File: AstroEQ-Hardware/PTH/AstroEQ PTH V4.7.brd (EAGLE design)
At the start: 100 x 66 mm, 54 parts, among them IC1 DIP40-SOCKET, IC2 DIP20-SOCKET, IC3 78L05, J2 DNI, J3 DNI, M1 Motor Driver, M2 Motor Driver, Q1 NTR4501NT1G, X1 16MHz, X2 12MHz

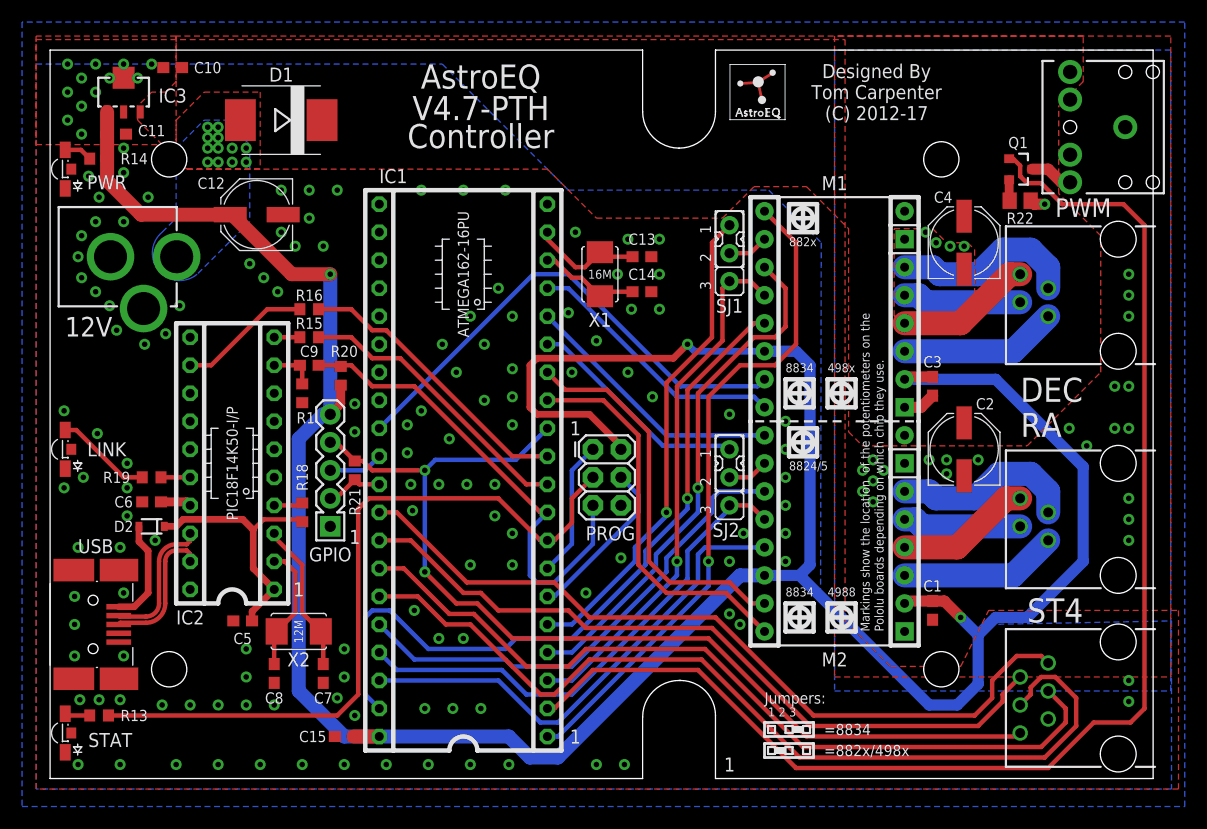
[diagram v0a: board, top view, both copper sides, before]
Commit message: Update AstroEQ PTH/SMD Schematics
1. Tidy up the schematics, add a frame, and improve labelling of nets
2. Add extra textual documentation to the PCB to label the various extra IO pins.
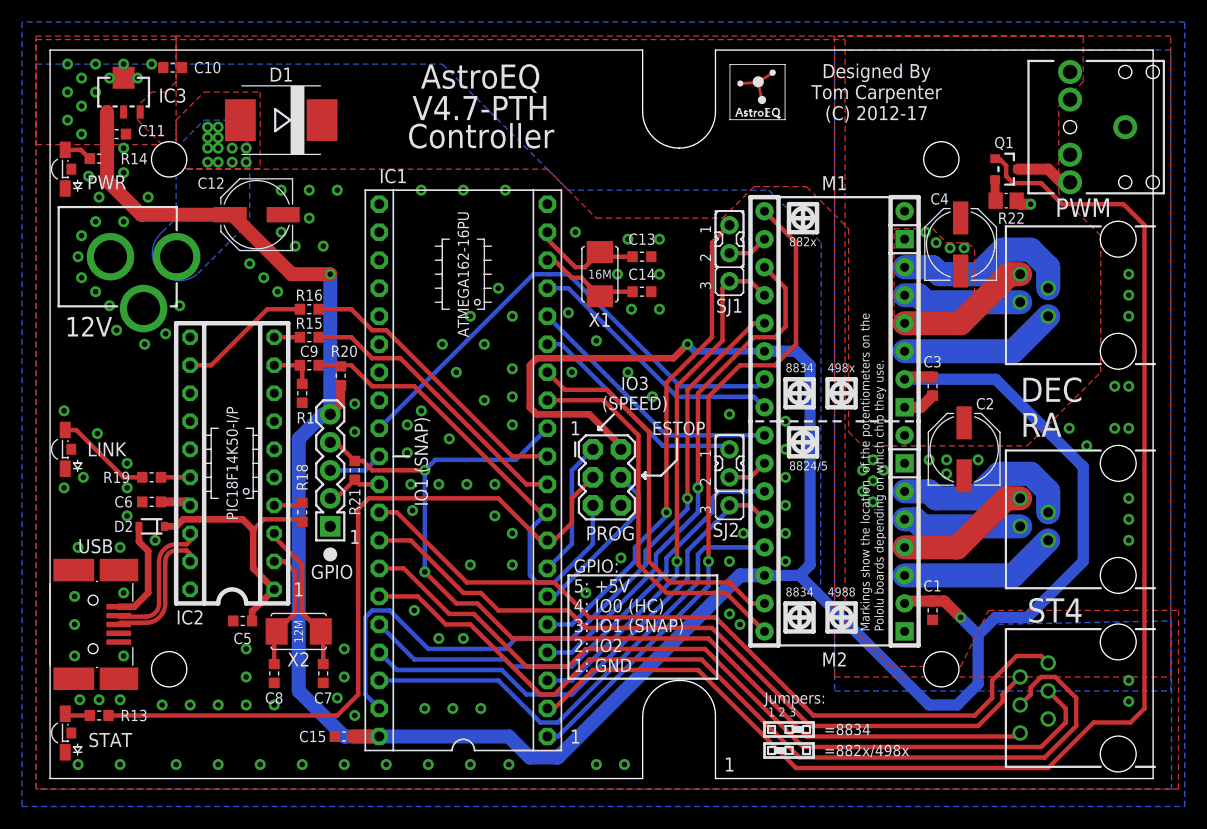
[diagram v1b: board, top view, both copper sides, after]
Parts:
- IC1: device atmel:DIL40-SKT -> atmel:DIL40
- moved Q1 1.27 mm to (86.7, 55.2)
- moved R22 1.27 mm to (86.7, 52.4)
- moved C4 0.35 mm to (82.5, 48.4)
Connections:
- net MISO renamed IO3-MISO
- net MOSI renamed ESTOP-MOSI
- net PWM-OUT renamed PWM-OD
- net SCLK renamed STAT-SCLK
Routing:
- net PWM: track 120.6 -> 121.9 mm
- net PWM-OD: track 3.92 -> 5.19 mm
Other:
- board text added: "ESTOP"
- board text added: "For DIY, use "AstroEQ PTH V4.6""
- board text added: "GPIO: 5: +5V 4: IO0 (HC) 3: IO1 (SNAP) 2: IO2 1: GND"
- board text added: "IO1 (SNAP)"
- board text added: "IO3 (SPEED)"
- board text removed: "For DIY, use "AstroEQ PTH MK3""
